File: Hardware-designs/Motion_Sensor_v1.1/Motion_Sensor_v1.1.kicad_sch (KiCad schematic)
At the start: 37 parts, among them J1 UART, J2 Bat, J3 USB_C, J4 I2C, J5 I2C, Q1 AO3407A, SW2 PTS526 SM15 SMTR2 LFS, U1 ESP32-WROOM-32, U2 TP4057, U4 MCP1700

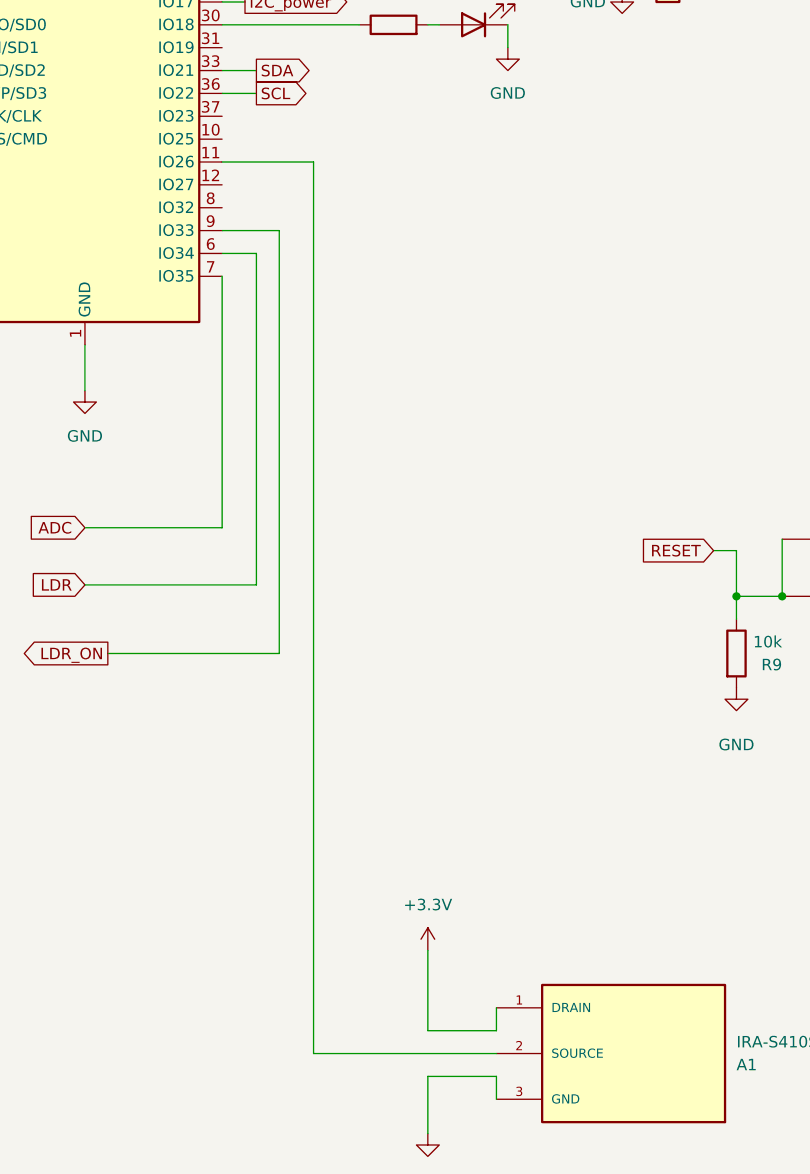
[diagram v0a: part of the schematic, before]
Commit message: Magnetic Sensor AAA battery version added
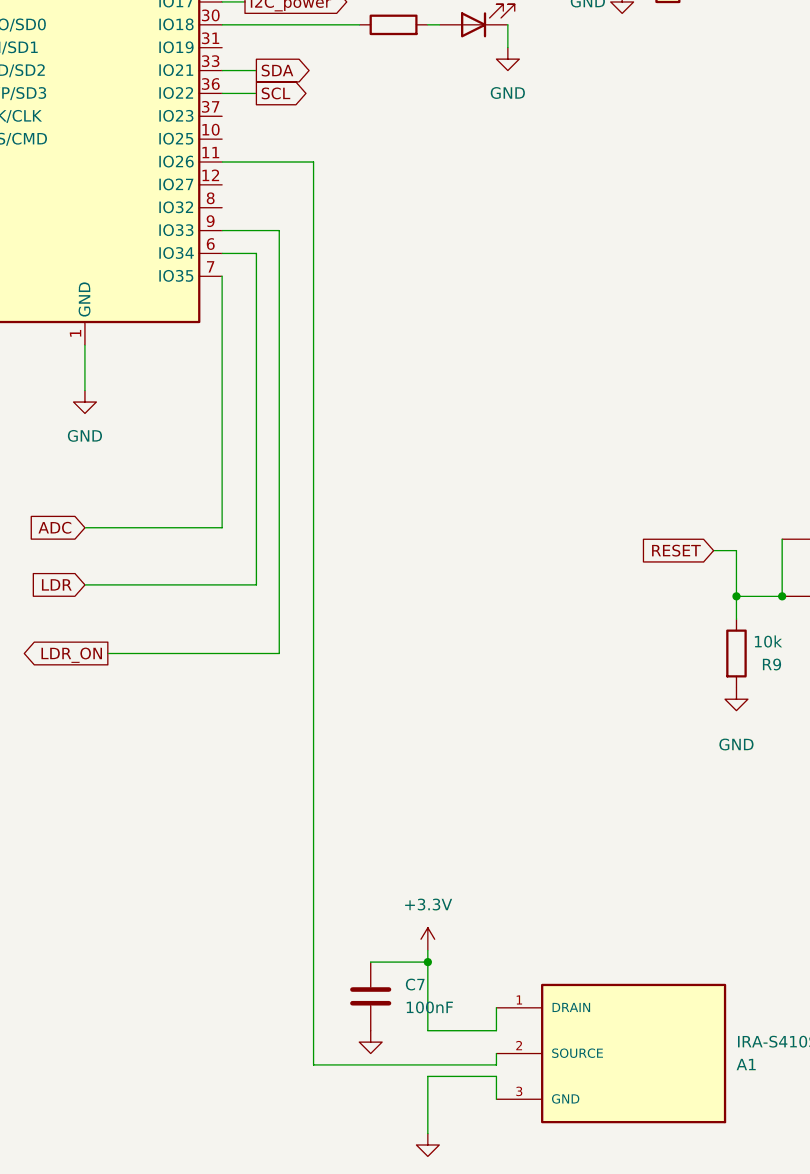
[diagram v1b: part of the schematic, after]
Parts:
- added C7: 100nF, Capacitor_SMD:C_0805_2012Metric_Pad1.18x1.45mm_HandSolder, symbol Device:C
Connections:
- net +3.3V: now also C7.1
- net GND: now also C7.2
